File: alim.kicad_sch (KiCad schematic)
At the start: 10 parts

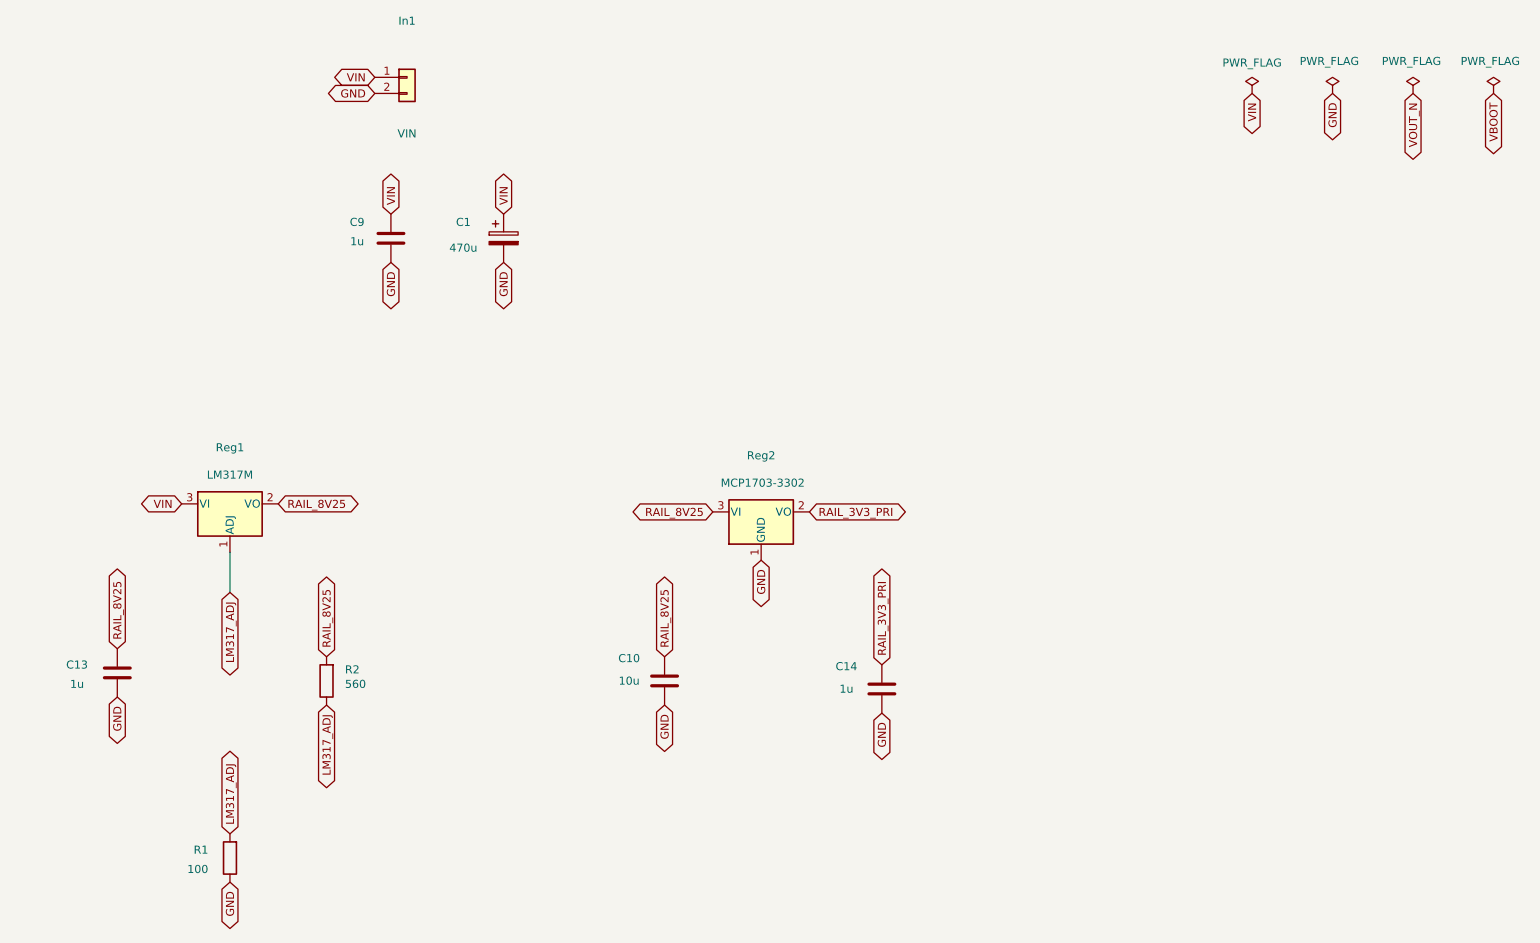
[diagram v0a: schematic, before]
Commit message: Isolation C2000 réelle (GND_CTRL/3V3_CTRL) + feuille Polarisation (HV_BIAS actif 0-90V)
- U3/U4/U5/U7/U8/U9 migrés côté contrôle vers GND_CTRL/3V3_CTRL (isolation
  du C2000 réellement effective, plus seulement nominale)
- Connecteurs CpuOut/CpuIn agrandis 2x04→2x08 (16 broches), marge pour
  futurs signaux et compatibilité avec d'autres cartes
- Nouvelle feuille polarisation.kicad_sch : pilotage actif de HV_BIAS
  (point de polarisation du secondaire flottant) depuis une alimentation
  400V externe — source de courant 300µA (BSS127I+MMBT2222), MOSFET
  variable BSS127I piloté par PWM isolé (ISO7710), protection TVS +
  pull-up grille, retour mesure isolé (AMC0311R)
- Nouveaux symboles custom BSS127I/MMBT2222, empreinte SOIC_DWV partagée
  par les amplis isolés de la famille AMC03x1R/AMC03x2R

Co-Authored-By: Claude Sonnet 5 <noreply@anthropic.com>
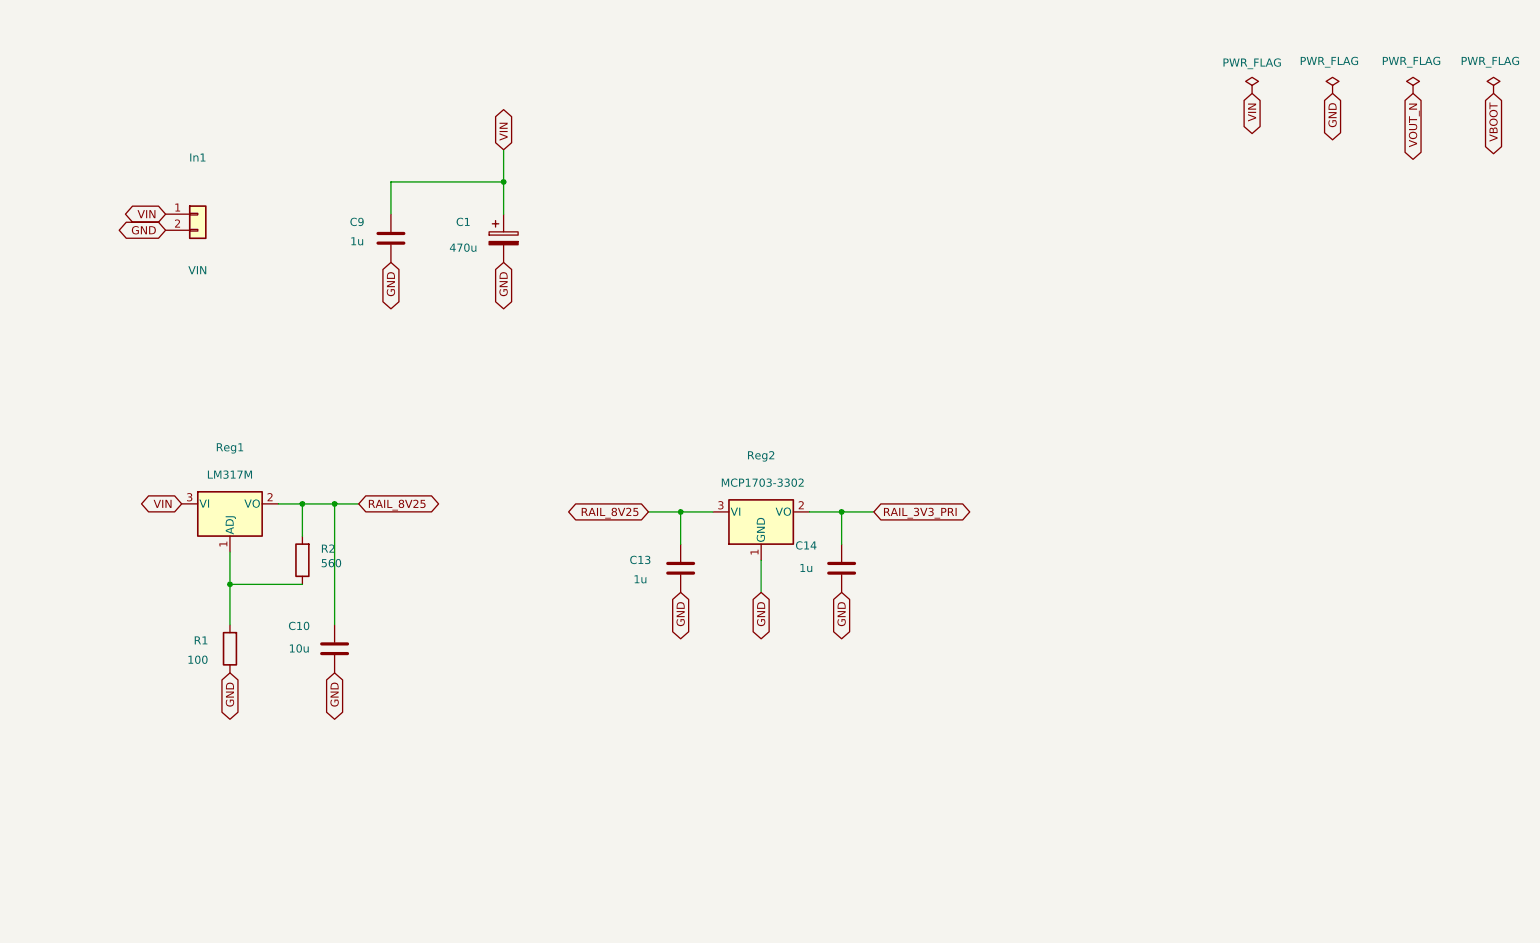
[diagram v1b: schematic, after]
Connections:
- net LM317_ADJ: no longer names the net of R1.2, R2.1, Reg1.1 (ADJ)
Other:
- moved on the sheet: C10, C13, C14, In1, R1, R2

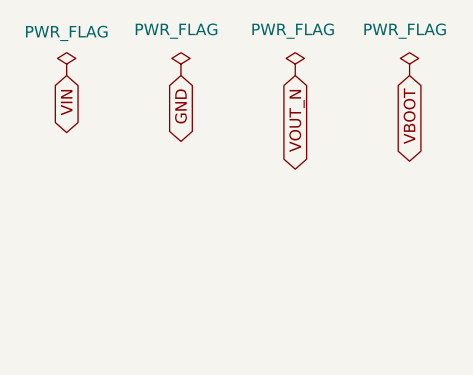
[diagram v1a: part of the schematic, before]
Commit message: Retours temperature/courant primaire isoles, isolation C2000 reelle, feuille Polarisation finalisee (80V, R26 corrige par simulation)
- U8 (AMC0311R) : retour temperature primaire (thermistance NTC) isole
- U9 (AMC0302R) : retour courant primaire (shunt R19) isole
- Migration GND_CTRL/3V3_CTRL : le C2000 externe recoit ses propres nets
  d'alimentation/masse isoles (U3/U4/U5/U7/U8/U9), connecteurs CpuOut/CpuIn
  agrandis a 16 broches
- Feuille polarisation.kicad_sch reprise en etiquettes globales uniquement
  (plus de fils explicites) et alignee sur la grille 1.27mm
- Source de courant Q3/Q4/R25/R26 simplifiee a un rail fixe 80V (HV80_IN,
  ex-400V) ; R26 corrige de 2M7 a 75k apres simulation SPICE (ngspice,
  modeles reels Diodes Inc.) qui a revele que le montage se comporte
  comme une resistance plutot qu'une source plate - voir 00-intention-
  conception.md §15bis
- Nouveau script bom_family_report.py (remplace BOMconverter.py) :
  nomenclature groupee par famille, sans dependance externe, lit soit le
  netlist XML legacy d'Eeschema soit un CSV kicad-cli
- README.md : image du schema integree
- Mise a jour 00-intention-conception.md (§13-15bis)

Co-Authored-By: Claude Sonnet 5 <noreply@anthropic.com>
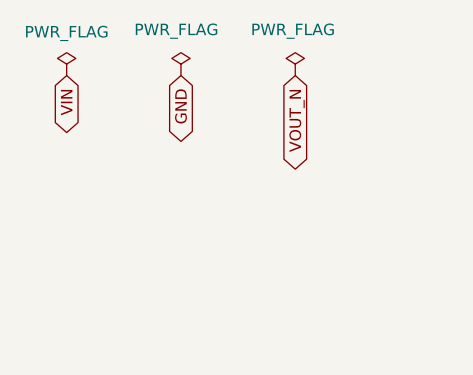
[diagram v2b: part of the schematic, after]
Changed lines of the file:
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@@
-		)
-	)
-	(global_label "VBOOT"
-		(shape bidirectional)
-		(at 262.89 31.75 270)
-		(fields_autoplaced yes)
-		(effects
-			(font
-				(size 1.27 1.27)
-			)
-			(justify right)
-		)
-		(property "Intersheetrefs" "${INTERSHEET_REFS}"
-			(at 262.89 31.75 0)
-			(hide yes)
-			(show_name no)
-			(do_not_autoplace no)
-			(effects
-				(font
-					(size 1.27 1.27)
-				)
-			)
 		)
 	)
@@
 					(unit 1)
 				)
-			)
-		)
-	)
-	(symbol
-		(lib_id "power:PWR_FLAG")
-		(at 262.89 31.75 0)
-		(unit 1)
-		(body_style 1)
-		(exclude_from_sim no)
-		(in_bom yes)
-		(on_board yes)
-		(in_pos_files yes)
-		(dnp no)
-		(property "Reference" "#FLGVBOOT01"
-			(at 262.89 33.65 0)
-			(hide yes)
-			(show_name no)
-			(do_not_autoplace no)
-			(effects
-				(font
-					(size 1.27 1.27)
-				)
-			)
-		)
-		(property "Value" "PWR_FLAG"
-			(at 262.382 26.67 0)
-			(show_name no)
-			(do_not_autoplace no)
-			(effects
-				(font
-					(size 1.27 1.27)
-				)
-			)
-		)
-		(property "Footprint" ""
-			(at 262.89 31.75 0)
-			(show_name no)
-			(do_not_autoplace no)
-			(effects
-				(font
-					(size 1.27 1.27)
-				)
-			)
-		)
-		(property "Datasheet" ""
-			(at 262.89 31.75 0)
-			(show_name no)
-			(do_not_autoplace no)
-			(effects
-				(font
-					(size 1.27 1.27)
-				)
-			)
-		)
-		(property "Description" ""
-			(at 262.89 31.75 0)
-			(show_name no)
-			(do_not_autoplace no)
-			(effects
-				(font
-					(size 1.27 1.27)
-				)
-			)
-		)
-		(pin "1"
-		)
-		(instances
-			(project "alim-flyback-filament"
-				(path "/c8449ac7-87b3-4a93-889f-06dd686c5aff/4222d5eb-1966-4c25-91d0-a2dfc8338ee2"
-					(reference "#FLGVBOOT01")
-					(unit 1)
-				)

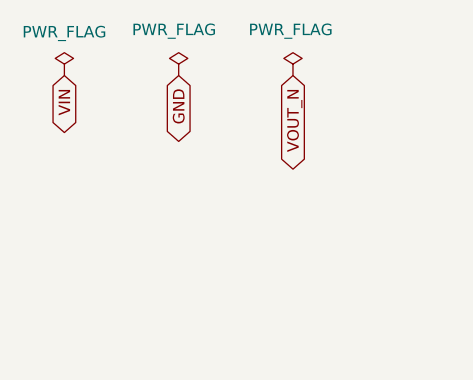
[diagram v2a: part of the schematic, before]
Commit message: Validation 18,9W + redressement synchrone : UCC24612 (U12) remplace U2/U4, clamp D4 ajouté
Simulation SPICE à la cible réelle (18,9W, pas les 10W de validation initiale) :
Vds_Q2 dépasse 100V dès Vin=20V sans clamp secondaire, indépendamment du
redresseur. UCC24612 amène +5pts de rendement mais ne corrige pas la
surtension -- D4 (SMCJ54A) ajouté pour ça. U2/U4 retirés (timing firmware
aveugle, remplacé par la détection Vds de l'UCC24612).

Co-Authored-By: Claude Sonnet 5 <noreply@anthropic.com>
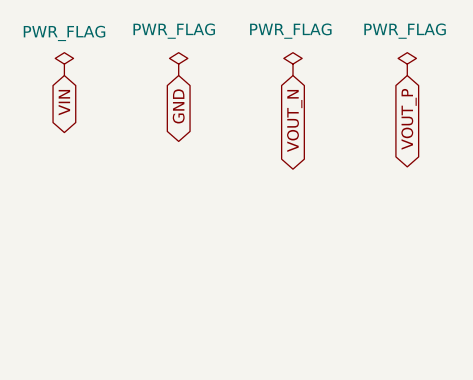
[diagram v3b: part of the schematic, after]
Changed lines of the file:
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@@
+		)
+	)
+	(global_label "VOUT_P"
+		(shape bidirectional)
+		(at 262.89 31.75 270)
+		(fields_autoplaced yes)
+		(effects
+			(font
+				(size 1.27 1.27)
+			)
+			(justify right)
+		)
+		(property "Intersheetrefs" "${INTERSHEET_REFS}"
+			(at 262.89 31.75 0)
+			(hide yes)
+			(show_name no)
+			(do_not_autoplace no)
+			(effects
+				(font
+					(size 1.27 1.27)
+				)
+			)
 		)
 	)
@@
 					(unit 1)
 				)
+			)
+		)
+	)
+	(symbol
+		(lib_id "power:PWR_FLAG")
+		(at 262.89 31.75 0)
+		(unit 1)
+		(body_style 1)
+		(exclude_from_sim no)
+		(in_bom yes)
+		(on_board yes)
+		(in_pos_files yes)
+		(dnp no)
+		(property "Reference" "#FLGVOUT_P01"
+			(at 262.89 33.65 0)
+			(hide yes)
+			(show_name no)
+			(do_not_autoplace no)
+			(effects
+				(font
+					(size 1.27 1.27)
+				)
+			)
+		)
+		(property "Value" "PWR_FLAG"
+			(at 262.636 26.67 0)
+			(show_name no)
+			(do_not_autoplace no)
+			(effects
+				(font
+					(size 1.27 1.27)
+				)
+			)
+		)
+		(property "Footprint" ""
+			(at 262.89 31.75 0)
+			(show_name no)
+			(do_not_autoplace no)
+			(effects
+				(font
+					(size 1.27 1.27)
+				)
+			)
+		)
+		(property "Datasheet" ""
+			(at 262.89 31.75 0)
+			(show_name no)
+			(do_not_autoplace no)
+			(effects
+				(font
+					(size 1.27 1.27)
+				)
+			)
+		)
+		(property "Description" ""
+			(at 262.89 31.75 0)
+			(show_name no)
+			(do_not_autoplace no)
+			(effects
+				(font
+					(size 1.27 1.27)
+				)
+			)
+		)
+		(pin "1"
+		)
+		(instances
+			(project "alim-flyback-filament"
+				(path "/c8449ac7-87b3-4a93-889f-06dd686c5aff/4222d5eb-1966-4c25-91d0-a2dfc8338ee2"
+					(reference "#FLGVOUT_P01")
+					(unit 1)
+				)

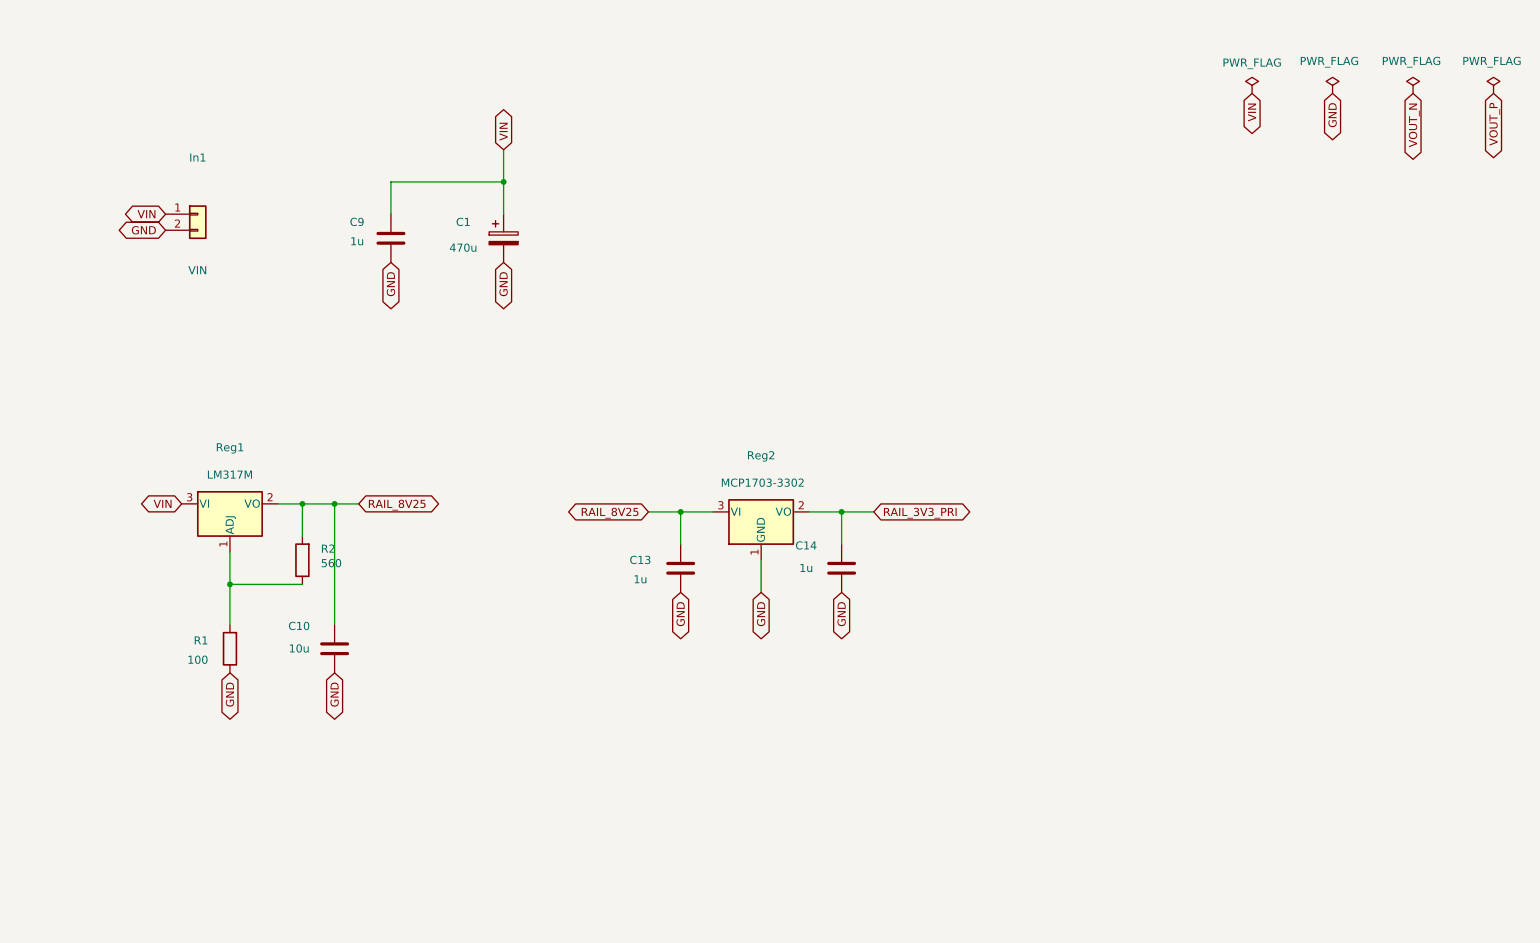
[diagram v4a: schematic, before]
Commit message: Ajoute F1 (fusible VIN) et D2 (TVS RAIL_8V25), documente le plan d'isolation
Deux composants poses par l'utilisateur dans alim.kicad_sch pour fermer
les chemins 1 et 2 du confinement de defaut (doc/plan-isolation-4couches.md,
S8) : F1 en serie sur VIN, D2 (SMCJ10A) entre RAIL_8V25 et GND. Verifies
par calcul de position de broche (pas seulement par label) et par
rechargement standalone + hierarchie complete.

Nomenclature verifiee : D5/D6/D7/R30-R32 proposes par le plan
collisionnaient avec limitation-courant.kicad_sch (S19, posterieur au
commit de base du plan) -- corrige dans le plan, prochains reperes
libres D8/R35-R37. Documente dans S20 de 00-intention-conception.md.

Ignore aussi les exports BOM (KICAD-HT.txt/.xml), regeneres a chaque
passage, meme categorie que les rapports ERC/DRC.

Co-Authored-By: Claude Sonnet 5 <noreply@anthropic.com>
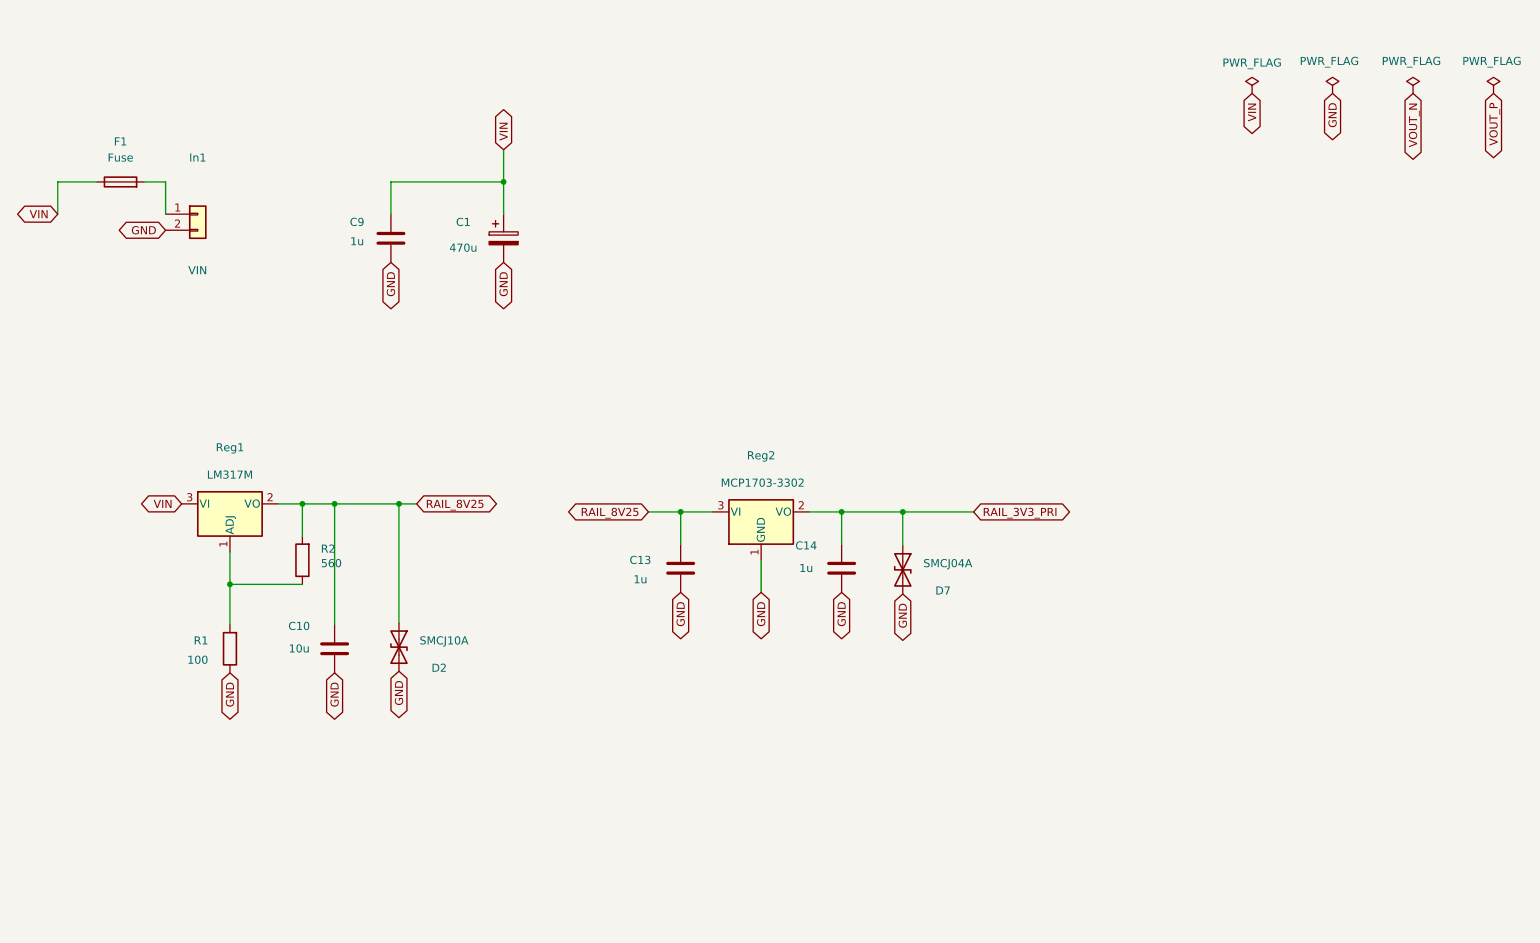
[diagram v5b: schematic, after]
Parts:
- added D2: SMCJ10A, Diode_SMD:D_SMC, symbol Device:D_TVS
- added D7: SMCJ04A, Diode_SMD:D_SMC, symbol Device:D_TVS
- added F1: Fuse, Fuse:Fuseholder_Clip-5x20mm_Littelfuse_111_Lateral_P18.80x5.00mm_D1.17mm_Horizontal, symbol Device:Fuse
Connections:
- net GND: now also D2.2 (A2), D7.2 (A2)
- net RAIL_3V3_PRI: now also D7.1 (A1)
- net RAIL_8V25: now also D2.1 (A1)
- net VIN: now also F1.1; no longer In1.1 (Pin_1)
- new net: F1.2, In1.1 (Pin_1)

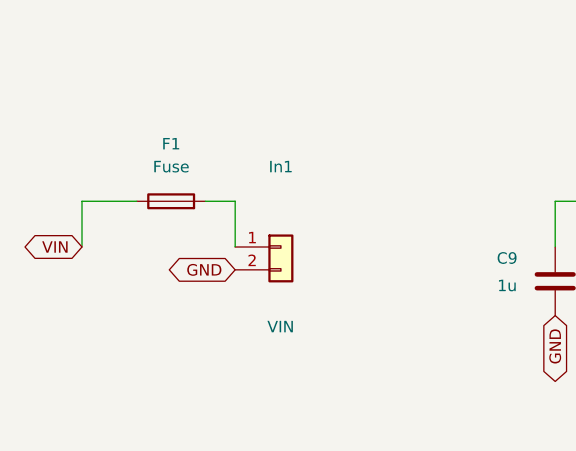
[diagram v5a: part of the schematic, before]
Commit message: Resistances de reference inter-domaines (3x1M par barriere), F1 a 3A
Ajoute les trois chaines de resistances 1M en serie (R35/R6/R36,
R37/R38/R39, R42/R41/R40) qui ferment le point ouvert du plan
d'isolation (S3) : reference DC entre les trois domaines sans degrader
la CMTI. Chaine plutot qu'une resistance unique -- un seul 0805 n'a que
0,8mm d'ecart cuivre entre ses pastilles, loin des 8,5mm vises.

F1 fixe a 3A. TVS directe sur VIN retiree de la liste : deja presente
sur KICAD-C2000-powershield, en amont au niveau systeme.

Nomenclature reverifiee sur tout le projet, aucune collision. Fichiers
touches revalides (equilibre parentheses conscient des chaines,
chargement standalone + hierarchie complete). Documente au S20 de
00-intention-conception.md et dans doc/plan-isolation-4couches.md
(recommandation d'origine << resistance unique sous l'isolateur >>
corrigee).

Co-Authored-By: Claude Sonnet 5 <noreply@anthropic.com>
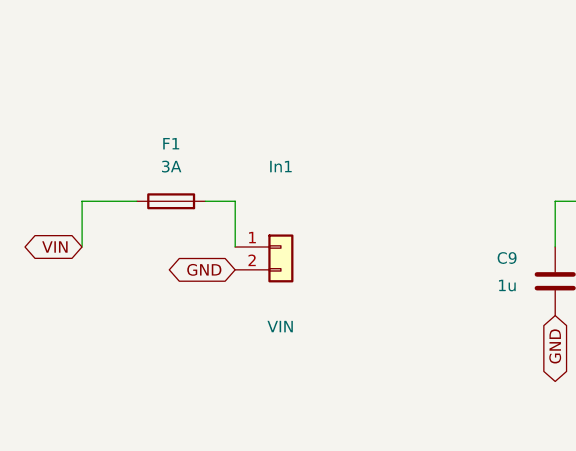
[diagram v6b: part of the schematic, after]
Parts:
- F1: value Fuse -> 3A
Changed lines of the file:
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@@
 			)
 		)
-		(property "Value" "Fuse"
+		(property "Value" "3A"
 			(at 46.228 41.91 90)
 			(show_name no)
